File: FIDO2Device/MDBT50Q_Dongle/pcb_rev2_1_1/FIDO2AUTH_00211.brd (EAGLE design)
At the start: 19.1 x 34.3 mm, 39 parts, among them CN1 TE-1734028, CN2 IF_4PIN, CN5 IF_2PIN_SOL, SW1 SKRPACE010, SW2 SKTADAE010, U1 MDBT50Q-P1M, U2 XC6206P332MR-G, U3 ATECC608A-MAHDA-S, X1 NX3215SA-32.768K

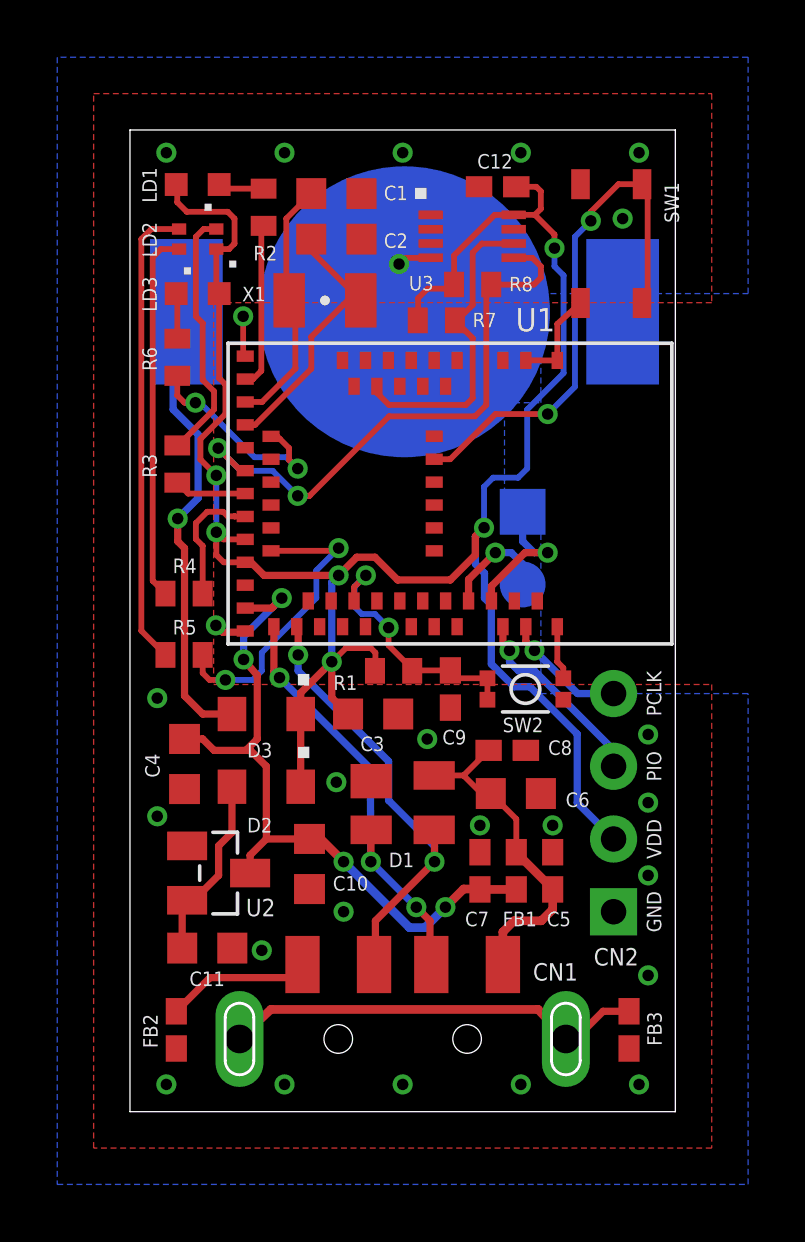
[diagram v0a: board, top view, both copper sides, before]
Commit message: プリント基板製作データを修正
・差動信号配線のパターンを改善
・ガーバー、centroid各データを再生成
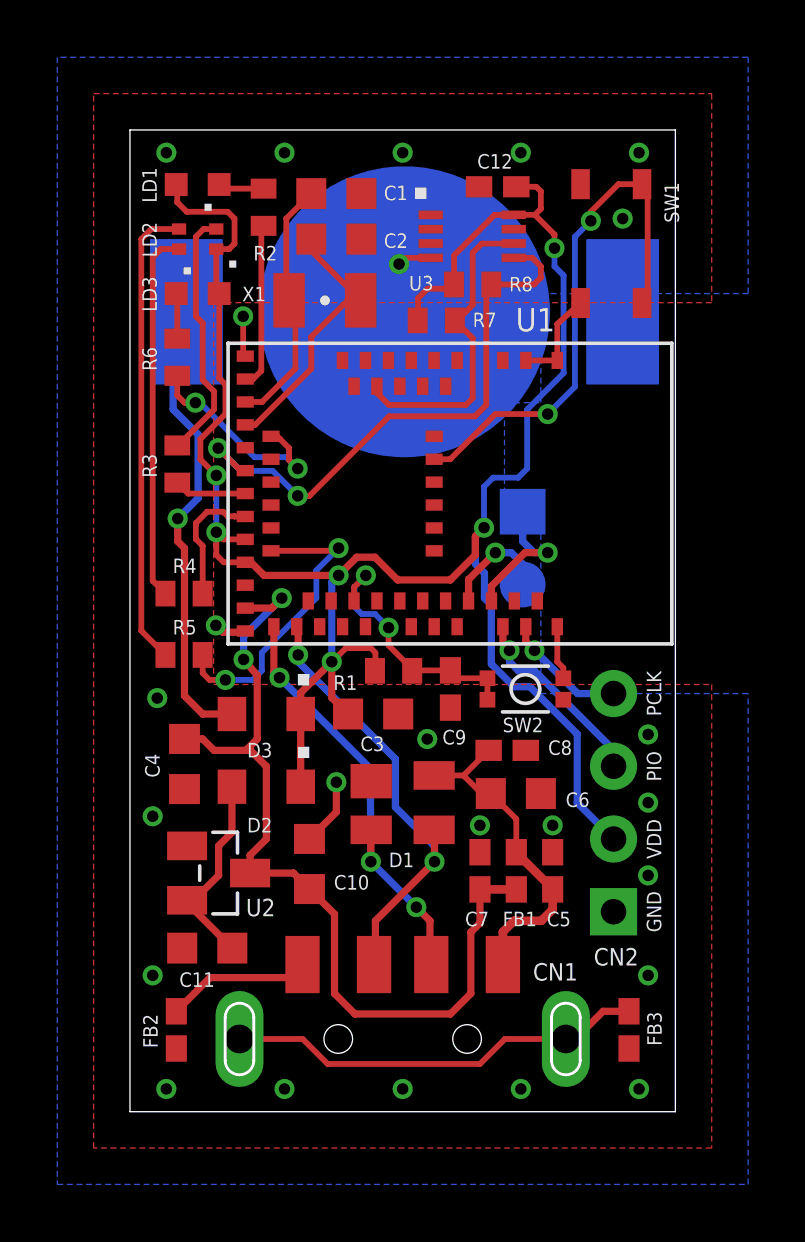
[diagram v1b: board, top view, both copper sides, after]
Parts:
- turned C10 to 90 degrees
- turned C11 to 180 degrees
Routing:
- net VBUS_NRF: track 25.5 -> 31.6 mm, vias 4 -> 2
- net 0V: track 9.17 -> 11.5 mm, vias 26 -> 25
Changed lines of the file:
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@@
 <attribute name="VALUE" x="-0.396875" y="9.8425" size="0.7112" layer="27" rot="R270"/>
 </element>
-<element name="C10" library="Parts" package="C0603K" value="1uF" x="6.270625" y="8.651875" smashed="yes" rot="R270">
-<attribute name="NAME" x="7.0866" y="7.7216" size="0.508" layer="25"/>
-<attribute name="VALUE" x="4.779375" y="9.451875" size="0.7112" layer="27" rot="R270"/>
-</element>
-<element name="C11" library="Parts" package="C0603K" value="1uF" x="2.69875" y="5.715" smashed="yes">
-<attribute name="NAME" x="3.311525" y="4.89585" size="0.508" layer="25" rot="R180"/>
-<attribute name="VALUE" x="1.89875" y="4.22375" size="0.7112" layer="27"/>
+<element name="C10" library="Parts" package="C0603K" value="1uF" x="6.270625" y="8.651875" smashed="yes" rot="R90">
+<attribute name="NAME" x="7.121525" y="7.756525" size="0.508" layer="25"/>
+<attribute name="VALUE" x="7.761875" y="7.851875" size="0.7112" layer="27" rot="R90"/>
+</element>
+<element name="C11" library="Parts" package="C0603K" value="1uF" x="2.69875" y="5.715" smashed="yes" rot="R180">
+<attribute name="NAME" x="2.9591" y="4.867275" size="0.508" layer="25" rot="R180"/>
+<attribute name="VALUE" x="3.49875" y="7.20625" size="0.7112" layer="27" rot="R180"/>
 </element>
 <element name="D2" library="Parts" package="SOD323-W" value="PMEG2005AEA,115" x="4.7625" y="11.350625" smashed="yes" rot="R180">
@@
 </polygon>
 <via x="3.952875" y="27.78125" extent="1-16" drill="0.4"/>
-<via x="9.525" y="0.9525" extent="1-16" drill="0.4"/>
+<via x="9.525" y="0.79375" extent="1-16" drill="0.4"/>
 <via x="10.38225" y="13.0175" extent="1-16" drill="0.4"/>
-<via x="13.6525" y="0.9525" extent="1-16" drill="0.4"/>
+<via x="13.6525" y="0.79375" extent="1-16" drill="0.4"/>
 <via x="3.000375" y="16.98625" extent="1-16" drill="0.4"/>
-<via x="5.3975" y="0.9525" extent="1-16" drill="0.4"/>
-<via x="4.60375" y="5.635625" extent="1-16" drill="0.4"/>
+<via x="5.3975" y="0.79375" extent="1-16" drill="0.4"/>
+<via x="0.79375" y="4.7625" extent="1-16" drill="0.4"/>
 <contactref element="CN2" pad="1"/>
 <via x="18.0975" y="4.7625" extent="1-16" drill="0.4"/>
 <via x="18.0975" y="10.795" extent="1-16" drill="0.4"/>
-<via x="17.78" y="0.9525" extent="1-16" drill="0.4"/>
-<via x="1.27" y="0.9525" extent="1-16" drill="0.4"/>
-<via x="7.46125" y="6.985" extent="1-16" drill="0.4"/>
+<via x="17.78" y="0.79375" extent="1-16" drill="0.4"/>
+<via x="1.27" y="0.79375" extent="1-16" drill="0.4"/>
 <via x="18.0975" y="13.17625" extent="1-16" drill="0.4"/>
 <via x="7.20725" y="11.509375" extent="1-16" drill="0.4"/>
@@
 <wire x1="10.503875" y1="29.82525" x2="9.616375" y2="29.82525" width="0.2032" layer="1"/>
 <wire x1="9.616375" y1="29.82525" x2="9.398" y2="29.606875" width="0.2032" layer="1"/>
-<via x="0.9525" y="10.31875" extent="1-16" drill="0.4"/>
+<via x="0.79375" y="10.31875" extent="1-16" drill="0.4"/>
 <via x="0.9525" y="14.44625" extent="1-16" drill="0.4"/>
+<wire x1="7.20725" y1="11.509375" x2="7.20725" y2="10.4635" width="0.254" layer="1"/>
+<wire x1="7.20725" y1="10.4635" x2="6.270625" y2="9.526875" width="0.254" layer="1"/>
 </signal>
 <signal name="XL1">
@@
 <contactref element="U2" pad="3"/>
 <contactref element="C10" pad="1"/>
-<via x="11.01725" y="7.14375" extent="1-16" drill="0.4"/>
-<via x="7.46125" y="8.73125" extent="1-16" drill="0.4"/>
 <via x="5.30225" y="17.93875" extent="1-16" drill="0.4"/>
 <via x="3.96875" y="15.795625" extent="1-16" drill="0.4"/>
-<wire x1="6.270625" y1="9.526875" x2="6.665625" y2="9.526875" width="0.3048" layer="1"/>
-<wire x1="6.665625" y1="9.526875" x2="7.46125" y2="8.73125" width="0.3048" layer="1"/>
-<wire x1="7.46125" y1="8.73125" x2="9.763125" y2="6.429375" width="0.3048" layer="16"/>
-<wire x1="12.159375" y1="7.699375" x2="12.22375" y2="7.76375" width="0.3048" layer="1"/>
 <wire x1="12.22375" y1="7.76375" x2="13.49375" y2="7.76375" width="0.3048" layer="1"/>
-<wire x1="12.159375" y1="7.699375" x2="12.08" y2="7.77875" width="0.3048" layer="1"/>
-<wire x1="9.763125" y1="6.429375" x2="10.302875" y2="6.429375" width="0.3048" layer="16"/>
-<wire x1="10.302875" y1="6.429375" x2="11.01725" y2="7.14375" width="0.3048" layer="16"/>
-<wire x1="12.08" y1="7.77875" x2="11.65225" y2="7.77875" width="0.3048" layer="1"/>
-<wire x1="11.65225" y1="7.77875" x2="11.01725" y2="7.14375" width="0.3048" layer="1"/>
 <wire x1="4.195625" y1="8.334375" x2="4.195625" y2="8.958125" width="0.254" layer="1"/>
 <wire x1="4.195625" y1="8.958125" x2="4.764375" y2="9.526875" width="0.254" layer="1"/>
-<wire x1="6.270625" y1="9.526875" x2="4.764375" y2="9.526875" width="0.254" layer="1"/>
 <wire x1="1.905" y1="13.019375" x2="2.538125" y2="13.019375" width="0.254" layer="1"/>
 <wire x1="2.538125" y1="13.019375" x2="2.936875" y2="12.620625" width="0.254" layer="1"/>
@@
 <wire x1="4.9535" y1="17.59" x2="4.026" y2="17.59" width="0.254" layer="1"/>
 <wire x1="3.96875" y1="16.60525" x2="5.30225" y2="17.93875" width="0.254" layer="16"/>
+<wire x1="4.195625" y1="8.334375" x2="5.713125" y2="8.334375" width="0.254" layer="1"/>
+<wire x1="5.713125" y1="8.334375" x2="6.270625" y2="7.776875" width="0.254" layer="1"/>
+<wire x1="7.14375" y1="4.1275" x2="7.14375" y2="6.90375" width="0.254" layer="1"/>
+<wire x1="7.14375" y1="6.90375" x2="6.270625" y2="7.776875" width="0.254" layer="1"/>
+<wire x1="7.14375" y1="4.1275" x2="7.858125" y2="3.413125" width="0.254" layer="1"/>
+<wire x1="11.191875" y1="3.413125" x2="11.90625" y2="4.1275" width="0.254" layer="1"/>
+<wire x1="11.90625" y1="4.1275" x2="11.90625" y2="6.270625" width="0.254" layer="1"/>
+<wire x1="11.90625" y1="6.270625" x2="12.22375" y2="6.588125" width="0.254" layer="1"/>
+<wire x1="12.22375" y1="6.588125" x2="12.22375" y2="7.76375" width="0.254" layer="1"/>
+<wire x1="7.858125" y1="3.413125" x2="11.191875" y2="3.413125" width="0.254" layer="1"/>
 </signal>
 <signal name="SWDCLK">
@@
 <via x="10.63625" y="8.73125" extent="1-16" drill="0.4"/>
 <via x="5.87375" y="15.954375" extent="1-16" drill="0.4"/>
-<wire x1="9.032875" y1="10.874375" x2="9.032875" y2="12.239625" width="0.254" layer="16"/>
 <wire x1="10.63625" y1="8.73125" x2="8.5725" y2="6.6675" width="0.254" layer="1"/>
 <wire x1="8.5725" y1="6.6675" x2="8.5725" y2="5.1875" width="0.254" layer="1"/>
@@
 <wire x1="10.63625" y1="8.73125" x2="10.63625" y2="9.83375" width="0.254" layer="1"/>
 <wire x1="10.63625" y1="9.83375" x2="10.625" y2="9.845" width="0.254" layer="1"/>
-<wire x1="9.032875" y1="10.874375" x2="10.63625" y2="9.271" width="0.254" layer="16"/>
+<wire x1="9.271" y1="10.63625" x2="10.63625" y2="9.271" width="0.254" layer="16"/>
 <wire x1="10.63625" y1="9.271" x2="10.63625" y2="8.73125" width="0.254" layer="16"/>
-<wire x1="9.032875" y1="12.239625" x2="5.87375" y2="15.39875" width="0.254" layer="16"/>
-<wire x1="5.87375" y1="15.954375" x2="5.87375" y2="15.39875" width="0.254" layer="16"/>
 <wire x1="5.87375" y1="15.954375" x2="5.87375" y2="16.89225" width="0.254" layer="1"/>
 <wire x1="5.87375" y1="16.89225" x2="5.826" y2="16.94" width="0.254" layer="1"/>
+<wire x1="9.271" y1="12.319" x2="5.87375" y2="15.71625" width="0.254" layer="16"/>
+<wire x1="5.87375" y1="15.71625" x2="5.87375" y2="15.954375" width="0.254" layer="16"/>
+<wire x1="9.271" y1="12.319" x2="9.271" y2="10.63625" width="0.254" layer="16"/>
 </signal>
 <signal name="D_N">
@@
 <contactref element="CN1" pad="FG1"/>
 <contactref element="CN1" pad="FG2"/>
-<wire x1="3.825" y1="2.54" x2="4.920375" y2="3.571875" width="0.3048" layer="1"/>
-<wire x1="4.920375" y1="3.571875" x2="14.256625" y2="3.571875" width="0.3048" layer="1"/>
-<wire x1="14.256625" y1="3.571875" x2="15.225" y2="2.54" width="0.3048" layer="1"/>
 <wire x1="17.43075" y1="3.5075" x2="16.525" y2="3.5075" width="0.254" layer="1"/>
 <wire x1="16.525" y1="3.5075" x2="15.5575" y2="2.54" width="0.254" layer="1"/>
 <wire x1="15.225" y1="2.54" x2="15.5575" y2="2.54" width="0.254" layer="1"/>
+<wire x1="3.825" y1="2.54" x2="6.0325" y2="2.54" width="0.2032" layer="1"/>
+<wire x1="6.0325" y1="2.54" x2="6.905625" y2="1.666875" width="0.2032" layer="1"/>
+<wire x1="6.905625" y1="1.666875" x2="12.22375" y2="1.666875" width="0.2032" layer="1"/>
+<wire x1="15.225" y1="2.54" x2="13.096875" y2="2.54" width="0.2032" layer="1"/>
+<wire x1="12.22375" y1="1.666875" x2="13.096875" y2="2.54" width="0.2032" layer="1"/>
 </signal>
 <signal name="LED2_R">
@@
 <wire x1="3.095625" y1="9.286875" x2="3.5625" y2="9.75375" width="0.254" layer="1"/>
 <wire x1="3.5625" y1="11.350625" x2="3.5625" y2="9.75375" width="0.254" layer="1"/>
-<wire x1="1.82375" y1="5.715" x2="1.82375" y2="7.2125" width="0.254" layer="1"/>
-<wire x1="1.82375" y1="7.2125" x2="1.995625" y2="7.384375" width="0.254" layer="1"/>
+<wire x1="2.225" y1="7.384375" x2="2.225" y2="7.06375" width="0.254" layer="1"/>
+<wire x1="2.225" y1="7.06375" x2="3.57375" y2="5.715" width="0.254" layer="1"/>
 </signal>
 <signal name="N$5">
